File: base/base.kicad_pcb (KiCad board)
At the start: 2 copper layers, 100 x 100 mm, 103 parts, among them J1 Screw_Terminal_01x02, J2 Out, Q2 MJD31C, Q3 IPD50R3K0CE, Q4 MJD31C, Q5 MMBTA42, Q6 MMBTA42, Q7 MMBTA42, Q8 MMBTA42, T1 FL2015-3LB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

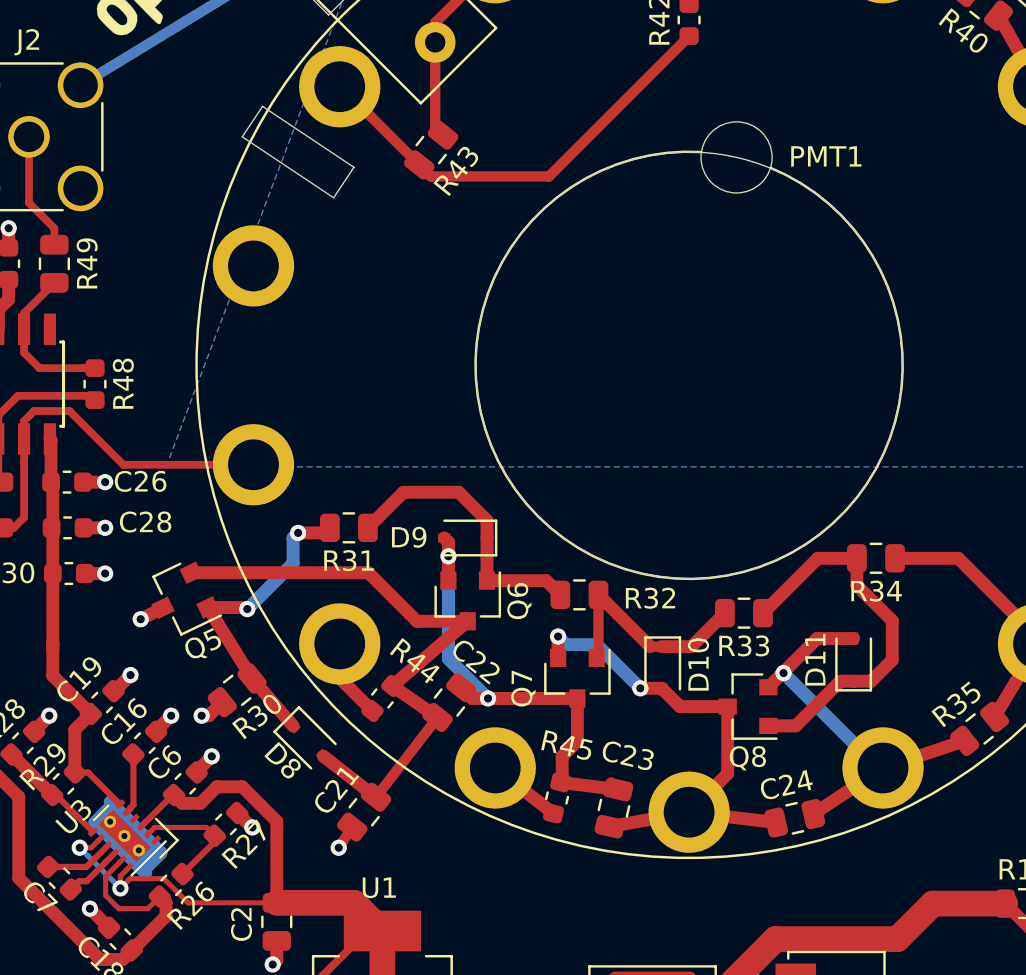
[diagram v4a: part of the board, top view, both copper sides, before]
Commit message: Fixed PMT hole size
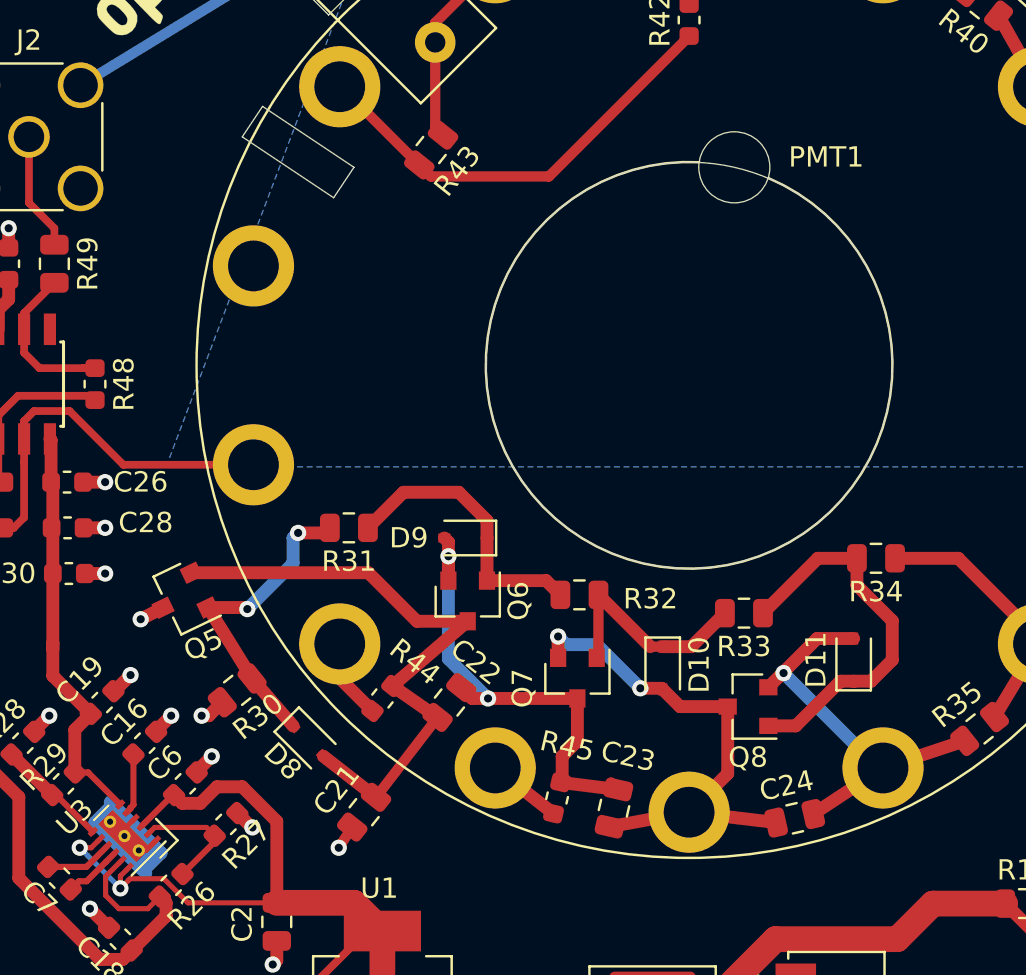
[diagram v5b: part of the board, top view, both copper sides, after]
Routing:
- net GND: track 154.0 -> 156.1 mm
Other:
- outline, holes or cut-outs redrawn
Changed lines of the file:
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@@
     (thickness 1.6)
     (drawings 54)
-    (tracks 528)
+    (tracks 532)
     (zones 0)
     (modules 103)
@@
   )
   (setup
-    (last_trace_width 0.635)
+    (last_trace_width 0.3048)
     (user_trace_width 0.254)
     (user_trace_width 0.3048)
@@
     (add_net "Net-(U4-Pad8)")
   )
+  (module B133D01:B133D01 (layer F.Cu)
+    (at 100 100)
+    (fp_text reference PMT1 (at 6.75 -10.25) (layer F.SilkS)
+      (effects (font (size 1 1) (thickness 0.15)))
+    )
+    (fp_text value B133D01 (at 5.08 36.33) (layer F.Fab)
+      (effects (font (size 1 1) (thickness 0.15)))
+    )
+    (fp_arc (start 0 0) (end 0.499999 -9.999999) (angle -339.8896839) (layer F.SilkS) (width 0.12))
+    (fp_circle (center 0 0) (end 24.25 0) (layer F.SilkS) (width 0.12))
+    (pad 1 thru_hole circle (at 0 -22) (size 4 4) (drill 2.5) (layers *.Cu *.Mask)
+      (net 34 "Net-(PMT1-Pad1)"))
+    (pad 2 thru_hole circle (at 9.545442 -19.821315) (size 4 4) (drill 2.5) (layers *.Cu *.Mask)
+      (net 35 "Net-(PMT1-Pad2)"))
+    (pad 3 thru_hole circle (at 17.200293 -13.716776) (size 4 4) (drill 2.5) (layers *.Cu *.Mask)
+      (net 36 "Net-(PMT1-Pad3)"))
+    (pad 4 thru_hole circle (at 21.448414 -4.895461) (size 4 4) (drill 2.5) (layers *.Cu *.Mask)
+      (net 37 "Net-(PMT1-Pad4)"))
+    (pad 5 thru_hole circle (at 21.448414 4.895461) (size 4 4) (drill 2.5) (layers *.Cu *.Mask)
+      (net 38 "Net-(PMT1-Pad5)"))
+    (pad 6 thru_hole circle (at 17.200293 13.716776) (size 4 4) (drill 2.5) (layers *.Cu *.Mask)
+      (net 39 "Net-(PMT1-Pad6)"))
+    (pad 7 thru_hole circle (at 9.545442 19.821315) (size 4 4) (drill 2.5) (layers *.Cu *.Mask)
+      (net 22 "Net-(C24-Pad1)"))
+    (pad 8 thru_hole circle (at 0 22) (size 4 4) (drill 2.5) (layers *.Cu *.Mask)
+      (net 21 "Net-(C23-Pad1)"))
+    (pad 9 thru_hole circle (at -9.545442 19.821315) (size 4 4) (drill 2.5) (layers *.Cu *.Mask)
+      (net 40 "Net-(PMT1-Pad9)"))
+    (pad 10 thru_hole circle (at -17.200293 13.716776) (size 4 4) (drill 2.5) (layers *.Cu *.Mask)
+      (net 41 "Net-(PMT1-Pad10)"))
+    (pad 11 thru_hole circle (at -21.448414 4.895461) (size 4 4) (drill 2.5) (layers *.Cu *.Mask)
+      (net 42 "Net-(PMT1-Pad11)"))
+    (pad 12 thru_hole circle (at -21.448414 -4.895461) (size 4 4) (drill 2.5) (layers *.Cu *.Mask)
+      (net 43 "Net-(PMT1-Pad12)"))
+    (pad 13 thru_hole circle (at -17.200293 -13.716776) (size 4 4) (drill 2.5) (layers *.Cu *.Mask)
+      (net 44 "Net-(PMT1-Pad13)"))
+    (pad 14 thru_hole circle (at -9.545442 -19.821315) (size 4 4) (drill 2.5) (layers *.Cu *.Mask)
+      (net 23 "Net-(C25-Pad1)"))
+    (pad "" np_thru_hole circle (at 2.225209 -9.749279) (size 3.5 3.5) (drill 3.5) (layers *.Cu *.Mask))
+  )
   (module Symbol:OSHW-Logo2_24.3x20mm_SilkScreen (layer F.Cu)
     (at 73.75 70.25 45)
@@
     )
   )
-  (module B133D01:B133D01 (layer F.Cu)
-    (at 100 100)
-    (fp_text reference PMT1 (at 6.75 -10.25) (layer F.SilkS)
-      (effects (font (size 1 1) (thickness 0.15)))
-    )
-    (fp_text value B133D01 (at 5.08 36.33) (layer F.Fab)
-      (effects (font (size 1 1) (thickness 0.15)))
-    )
-    (fp_arc (start 0 0) (end 0.599999 -10.499999) (angle -340.8606506) (layer F.SilkS) (width 0.12))
-    (fp_circle (center 0 0) (end 24.25 0) (layer F.SilkS) (width 0.12))
-    (pad 1 thru_hole circle (at 0 -22) (size 4 4) (drill 2.5) (layers *.Cu *.Mask)
-      (net 34 "Net-(PMT1-Pad1)"))
-    (pad 2 thru_hole circle (at 9.545442 -19.821315) (size 4 4) (drill 2.5) (layers *.Cu *.Mask)
-      (net 35 "Net-(PMT1-Pad2)"))
-    (pad 3 thru_hole circle (at 17.200293 -13.716776) (size 4 4) (drill 2.5) (layers *.Cu *.Mask)
-      (net 36 "Net-(PMT1-Pad3)"))
-    (pad 4 thru_hole circle (at 21.448414 -4.895461) (size 4 4) (drill 2.5) (layers *.Cu *.Mask)
-      (net 37 "Net-(PMT1-Pad4)"))
-    (pad 5 thru_hole circle (at 21.448414 4.895461) (size 4 4) (drill 2.5) (layers *.Cu *.Mask)
-      (net 38 "Net-(PMT1-Pad5)"))
-    (pad 6 thru_hole circle (at 17.200293 13.716776) (size 4 4) (drill 2.5) (layers *.Cu *.Mask)
-      (net 39 "Net-(PMT1-Pad6)"))
-    (pad 7 thru_hole circle (at 9.545442 19.821315) (size 4 4) (drill 2.5) (layers *.Cu *.Mask)
-      (net 22 "Net-(C24-Pad1)"))
-    (pad 8 thru_hole circle (at 0 22) (size 4 4) (drill 2.5) (layers *.Cu *.Mask)
-      (net 21 "Net-(C23-Pad1)"))
-    (pad 9 thru_hole circle (at -9.545442 19.821315) (size 4 4) (drill 2.5) (layers *.Cu *.Mask)
-      (net 40 "Net-(PMT1-Pad9)"))
-    (pad 10 thru_hole circle (at -17.200293 13.716776) (size 4 4) (drill 2.5) (layers *.Cu *.Mask)
-      (net 41 "Net-(PMT1-Pad10)"))
-    (pad 11 thru_hole circle (at -21.448414 4.895461) (size 4 4) (drill 2.5) (layers *.Cu *.Mask)
-      (net 42 "Net-(PMT1-Pad11)"))
-    (pad 12 thru_hole circle (at -21.448414 -4.895461) (size 4 4) (drill 2.5) (layers *.Cu *.Mask)
-      (net 43 "Net-(PMT1-Pad12)"))
-    (pad 13 thru_hole circle (at -17.200293 -13.716776) (size 4 4) (drill 2.5) (layers *.Cu *.Mask)
-      (net 44 "Net-(PMT1-Pad13)"))
-    (pad 14 thru_hole circle (at -9.545442 -19.821315) (size 4 4) (drill 2.5) (layers *.Cu *.Mask)
-      (net 23 "Net-(C25-Pad1)"))
-    (pad "" np_thru_hole circle (at 2.33647 -10.236743) (size 3.5 3.5) (drill 3.5) (layers *.Cu *.Mask))
-  )
   (module Package_TO_SOT_SMD:TO-252-2 (layer F.Cu)
     (at 130.4 119 65)
@@
     )
   )
+  (gr_circle (center 100 100) (end 100 90) (layer Edge.Cuts) (width 0.05))
   (gr_line (start 118.75 71.25) (end 119.5 72) (layer Edge.Cuts) (width 0.05))
   (gr_line (start 121.25 68.75) (end 118.75 71.25) (layer Edge.Cuts) (width 0.05))
@@
   )
   (gr_circle (center 100 100) (end 127.518176 100) (layer B.Fab) (width 0.12))
-  (gr_circle (center 100 100) (end 100 110.5) (layer Edge.Cuts) (width 0.05))
   (gr_circle (center 100 100) (end 101 150) (layer Edge.Cuts) (width 0.05))
   (segment (start 115.0375 143.7875) (end 116.5 143.7875) (width 0.635) (layer F.Cu) (net 1))
@@
   (segment (start 64.5 94.2125) (end 64.5 93.25) (width 0.635) (layer F.Cu) (net 2))
   (segment (start 62.5 94.2125) (end 62.5 93.25) (width 0.635) (layer F.Cu) (net 2))
+  (segment (start 72.2 122.821447) (end 72.2 123.175) (width 0.254) (layer F.Cu) (net 2))
+  (segment (start 72.694975 122.326472) (end 72.2 122.821447) (width 0.254) (layer F.Cu) (net 2))
+  (segment (start 73.26066 123.882107) (end 72.907107 123.882107) (width 0.254) (layer F.Cu) (net 2))
+  (segment (start 73.755635 123.387132) (end 73.26066 123.882107) (width 0.254) (layer F.Cu) (net 2))
   (segment (start 83.5125 126.4625) (end 79.7 126.4625) (width 1.27) (layer F.Cu) (net 3))
   (segment (start 84.9 127.85) (end 83.5125 126.4625) (width 1.27) (layer F.Cu) (net 3))

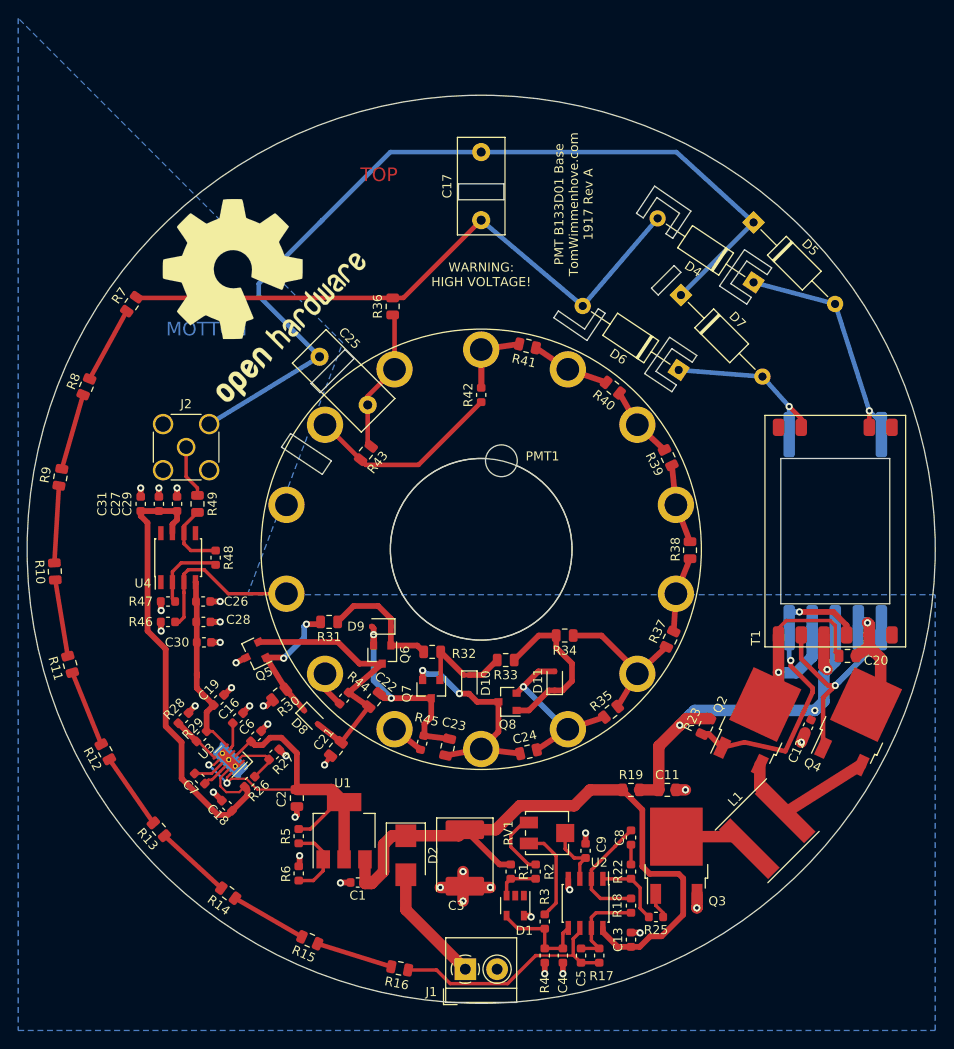
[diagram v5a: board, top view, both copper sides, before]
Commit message: Added testpoints
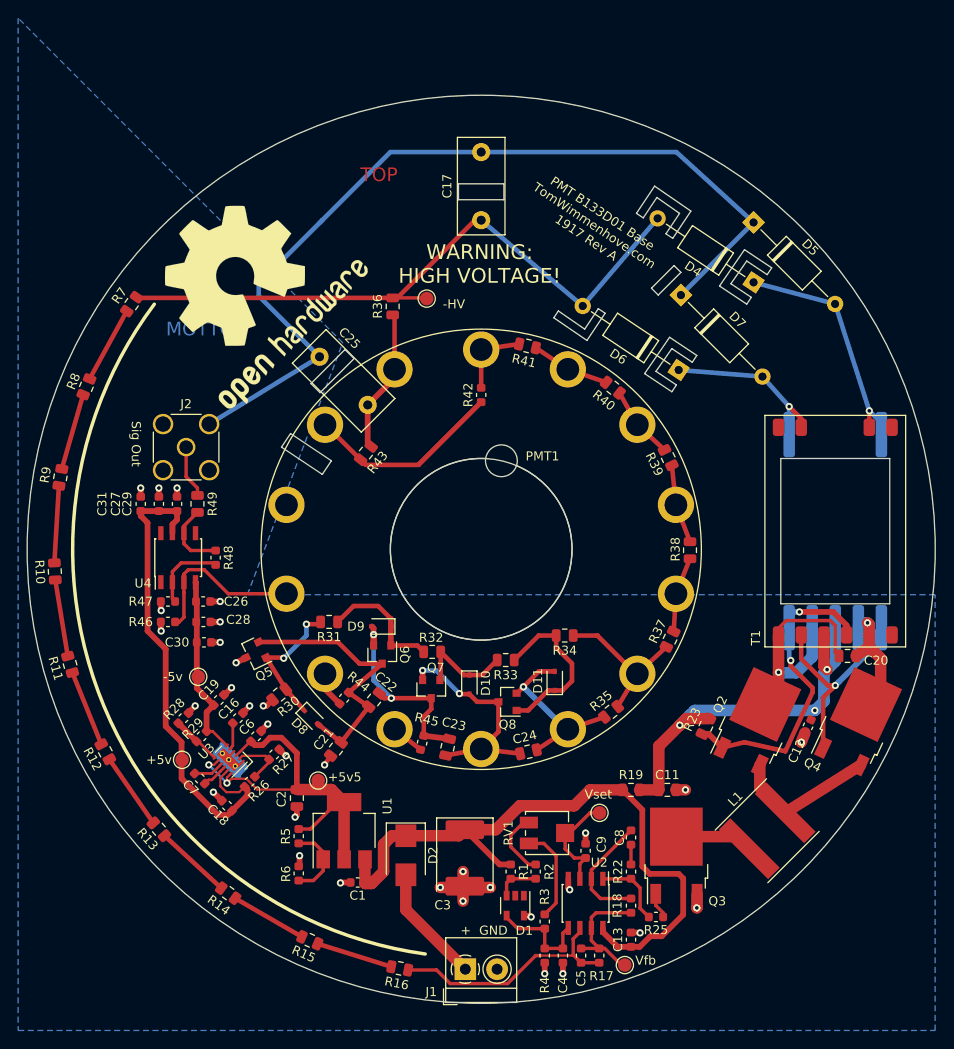
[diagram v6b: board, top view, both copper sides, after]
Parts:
- added TP1: +5v5, TestPoint:TestPoint_Pad_D1.5mm, F.Cu at (82.0, 125.5)
- added TP2: -HV, TestPoint:TestPoint_Pad_D1.5mm, F.Cu at (94.0, 72.4)
- added TP3: Vset, TestPoint:TestPoint_Pad_D1.5mm, F.Cu at (113.0, 129.0)
- added TP4: Vfb, TestPoint:TestPoint_Pad_D1.5mm, F.Cu at (115.8, 145.8)
- added TP5: +5v, TestPoint:TestPoint_Pad_D1.5mm, F.Cu at (67.1, 123.2)
- added TP6: -5v, TestPoint:TestPoint_Pad_D1.5mm, F.Cu at (68.8, 114.0)
- moved REF** 0.79 mm to (74.0, 71.0)
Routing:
- net Net-(PMT1-Pad13): track 22.0 -> 31.8 mm
- net Net-(C24-Pad1): track 25.6 -> 20.4 mm
- net Net-(C9-Pad1): track 6.98 -> 11.7 mm
- net Net-(PMT1-Pad1): track 12.5 -> 8.44 mm
- net Net-(C2-Pad1): track 44.4 -> 48.2 mm
- net -HV: track 68.9 -> 72.7 mm
- net Net-(C5-Pad2): track 10.4 -> 13.9 mm
- net Net-(D9-Pad1): track 14.0 -> 17.0 mm
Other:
- board text added: "+"
- board text added: "GND"
- board text added: "Sig Out"

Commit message: Added transformer 3d model
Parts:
- T1: footprint FL2015-3LB:FL2015-3LB -> FL2015-3LB:FL2015-4LB
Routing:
- net +12V: track 73.5 -> 70.5 mm
- net GND: vias 33 -> 46
- added copper zone on F.Cu, net GND
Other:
- board text added: "+12"
- board text removed: "+"
